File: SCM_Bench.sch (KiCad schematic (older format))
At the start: 22 parts, among them J1 Conn_Coaxial, J101 Conn_02x20_Odd_Even, J102 Conn_02x07_Odd_Even, J103 Conn_02x07_Odd_Even, J2 Conn_Coaxial, J3 Conn_Coaxial, J4 Conn_Coaxial, J5 Conn_Coaxial, J6 Conn_Coaxial, SW101 SW_Push, U101 ASDMB-xxxMHz

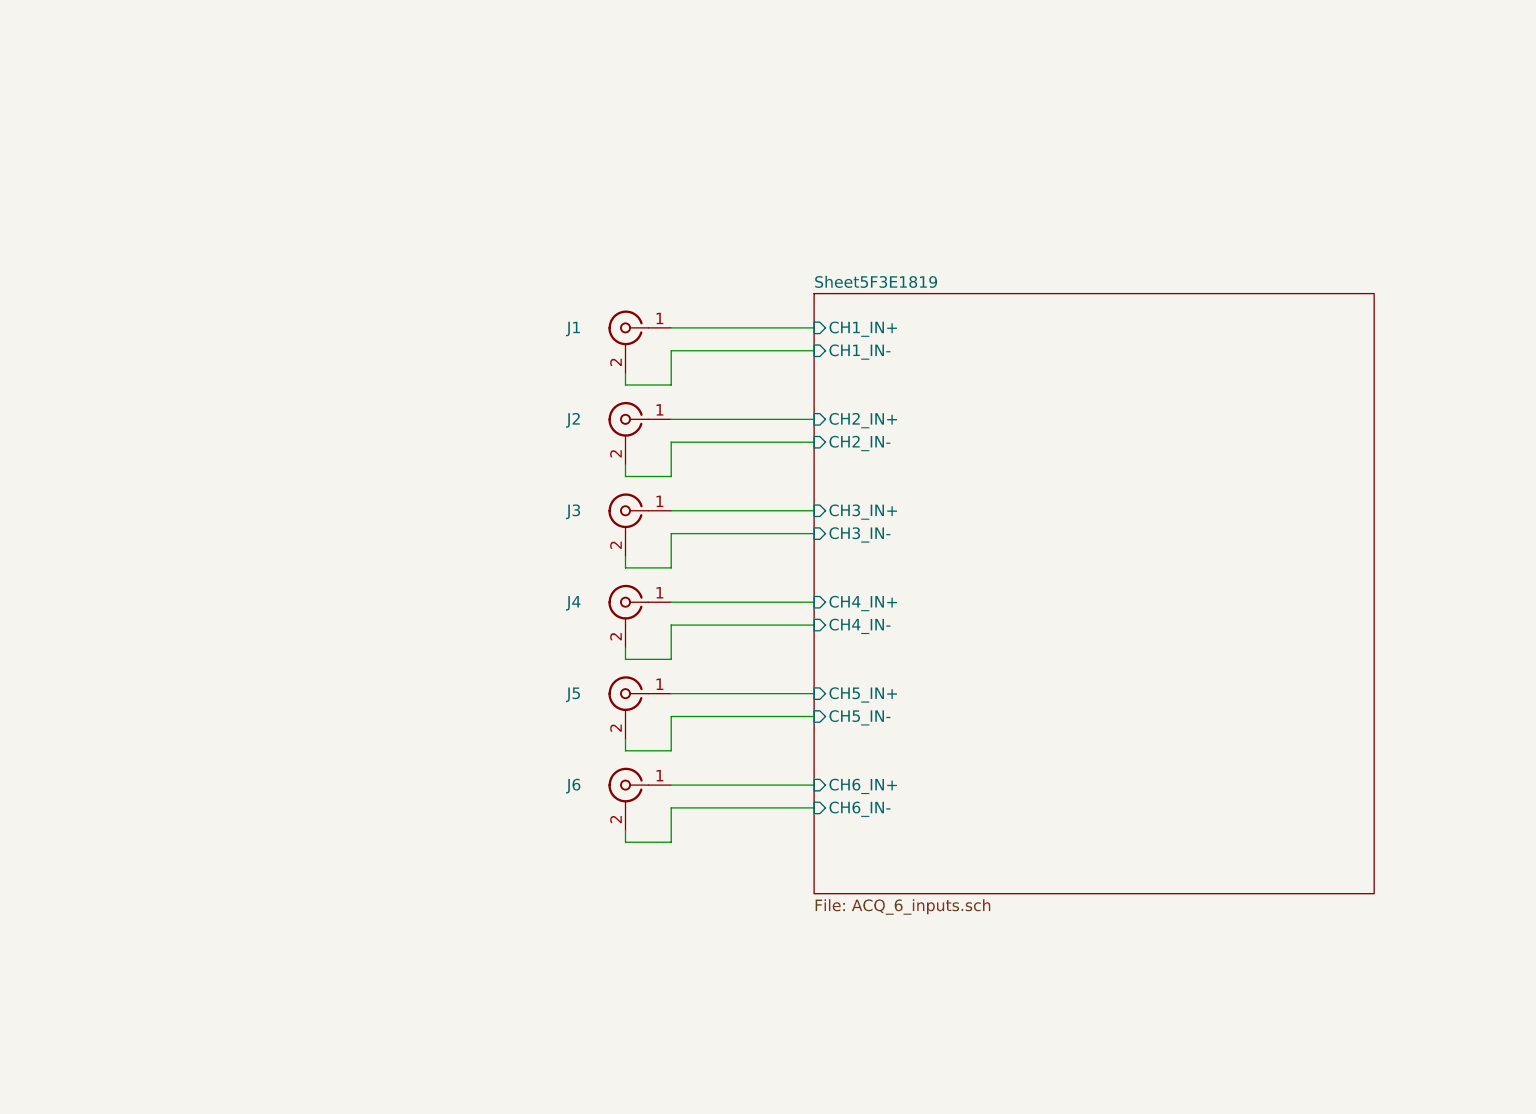
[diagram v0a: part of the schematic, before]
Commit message: Layout done for ADC + LVDS and DAC -> FPGA
Signed-off-by: Alexis Jeandet <alexis.jeandet@member.fsf.org>
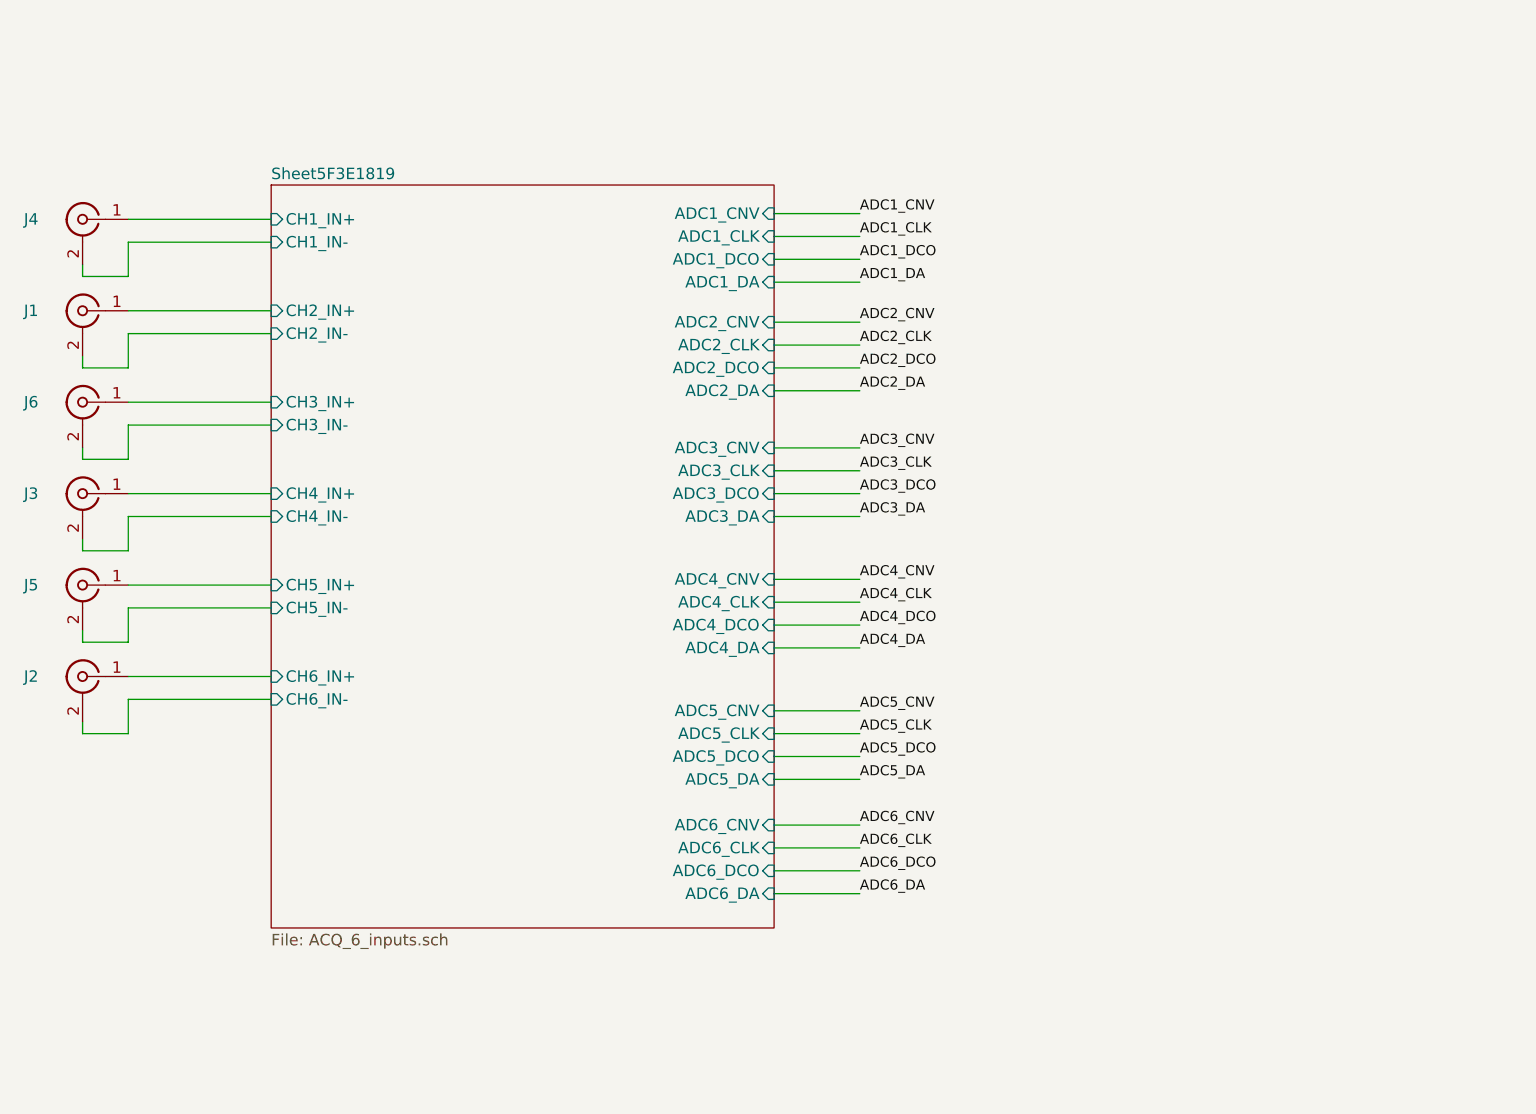
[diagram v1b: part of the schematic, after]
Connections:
- net Sheet5F3E1819/CH1_IN+: now also J4.1 (In); no longer J1.1 (In)
- net Sheet5F3E1819/CH1_IN-: now also J4.2 (Ext); no longer J1.2 (Ext)
- net Sheet5F3E1819/CH2_IN+: now also J1.1 (In); no longer J2.1 (In)
- net Sheet5F3E1819/CH2_IN-: now also J1.2 (Ext); no longer J2.2 (Ext)
- net Sheet5F3E1819/CH3_IN+: now also J6.1 (In); no longer J3.1 (In)
- net Sheet5F3E1819/CH3_IN-: now also J6.2 (Ext); no longer J3.2 (Ext)
- net Sheet5F3E1819/CH4_IN+: now also J3.1 (In); no longer J4.1 (In)
- net Sheet5F3E1819/CH4_IN-: now also J3.2 (Ext); no longer J4.2 (Ext)
- net Sheet5F3E1819/CH6_IN+: now also J2.1 (In); no longer J6.1 (In)
- net Sheet5F3E1819/CH6_IN-: now also J2.2 (Ext); no longer J6.2 (Ext)
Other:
- moved on the sheet: J1, J2, J3, J4, J5, J6

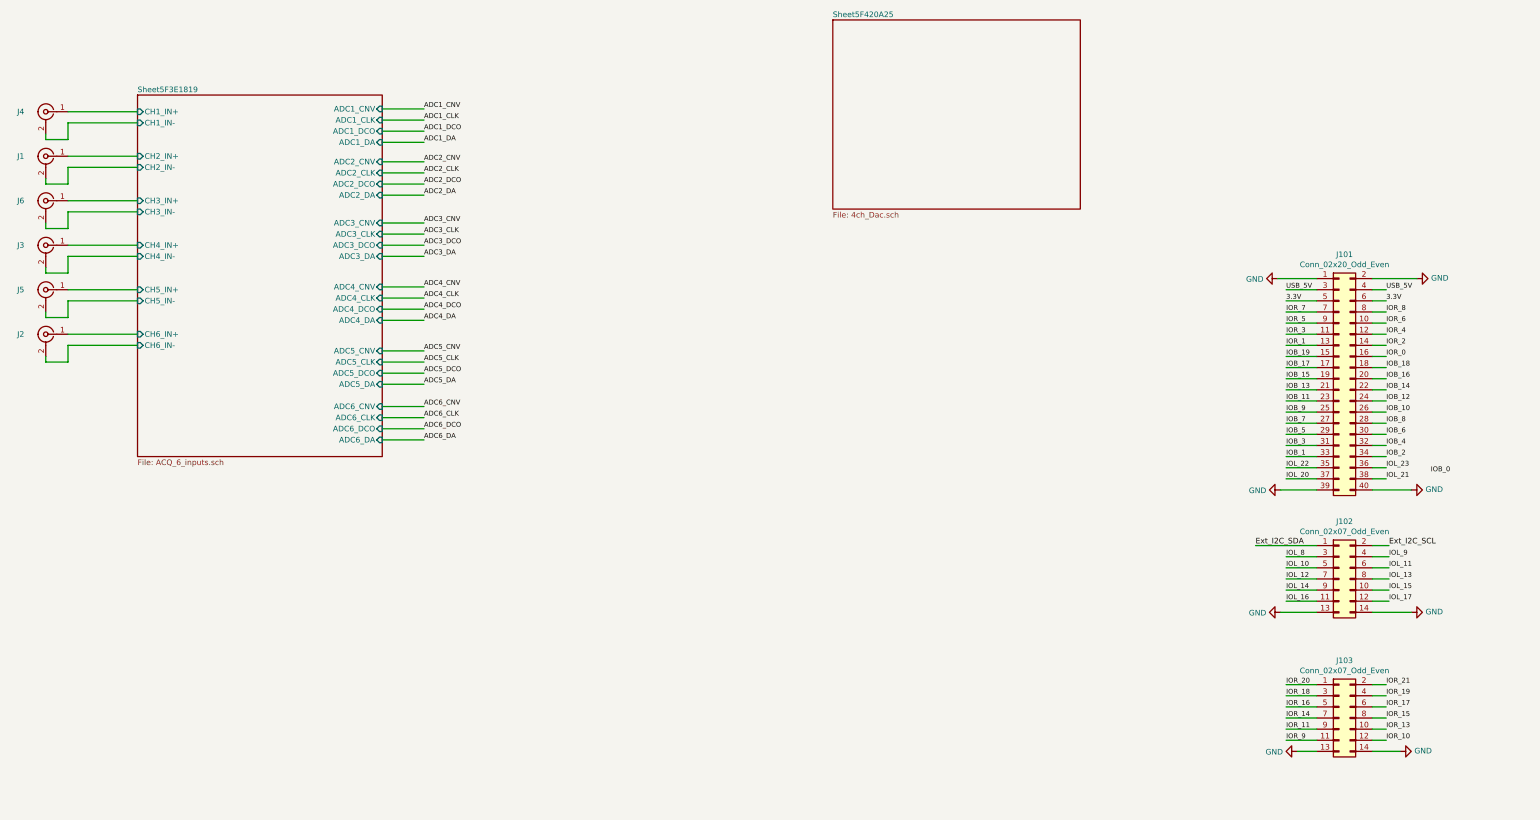
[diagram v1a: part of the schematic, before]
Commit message: Added #3.3V and #1.2V supply, completed ADC to USB board layout, added DAC FPGA to USB board bus.
Signed-off-by: Alexis Jeandet <alexis.jeandet@member.fsf.org>
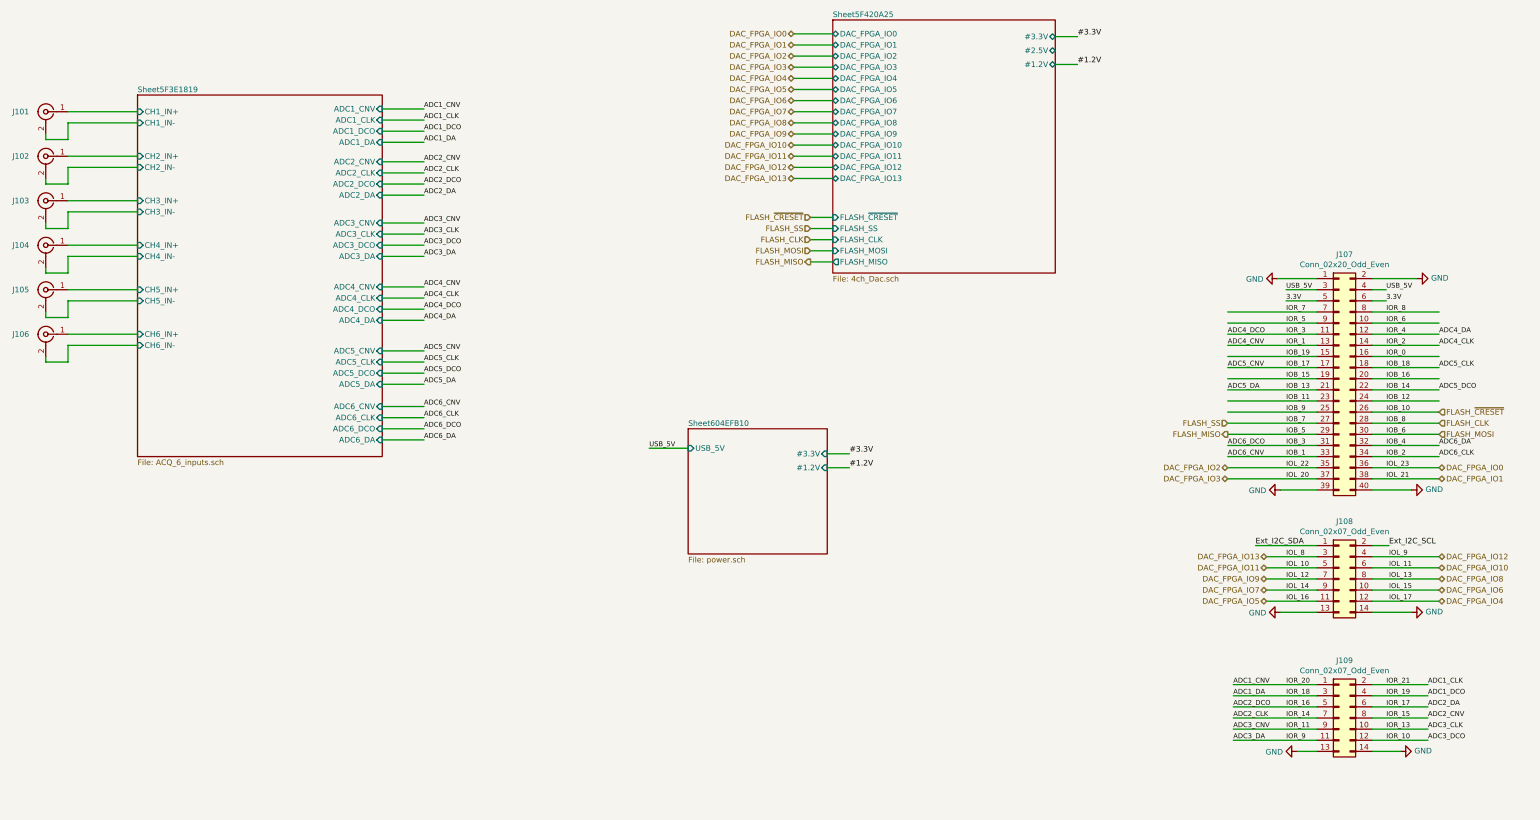
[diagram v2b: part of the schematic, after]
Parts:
- renumbered J4 to J101, J1 to J102, J6 to J103, J3 to J104, J5 to J105, J2 to J106, J101 to J107, J102 to J108, J103 to J109
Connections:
- net labels added: #1.2V, #3.3V, DAC_FPGA_IO0, DAC_FPGA_IO1, DAC_FPGA_IO10, DAC_FPGA_IO11, DAC_FPGA_IO12, DAC_FPGA_IO13, DAC_FPGA_IO2, DAC_FPGA_IO3, DAC_FPGA_IO4, DAC_FPGA_IO5, DAC_FPGA_IO6, DAC_FPGA_IO7, DAC_FPGA_IO8, DAC_FPGA_IO9, FLASH_CLK, FLASH_MISO, FLASH_MOSI, FLASH_SS, FLASH_~CRESET
- net labels removed: IOB_0
- wire segments 150 -> 174

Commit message: Layout complete, needs silk screen cleanup and few checks
Signed-off-by: Alexis Jeandet <alexis.jeandet@member.fsf.org>
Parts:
- removed C101, C102: 100nF, Capacitor_SMD:C_0402_1005Metric, symbol Device:C
- removed D101, D102: LED, Resistor_SMD:R_0603_1608Metric_Pad1.05x0.95mm_HandSolder, symbol Device:LED
- removed H101, H102: MountingHole, MountingHole:MountingHole_2.7mm_M2.5, symbol Mechanical:MountingHole
- removed R101, R102, R103: 2K2, Resistor_SMD:R_0402_1005Metric, symbol Device:R
- removed SW101: SW_Push, Button_Switch_SMD:SW_SPST_EVQPE1, symbol Switch:SW_Push
- removed U101: ASDMB-xxxMHz, Oscillator:Oscillator_SMD_Abracon_ASDMB-4Pin_2.5x2.0mm, symbol Oscillator:ASDMB-xxxMHz
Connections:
- net labels added: #1.8V, #2.5V, -5V, 2.5V, 5V, USB_3.3V
- wire segments 174 -> 161
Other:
- note added: "ADCs"
- note added: "DACs"
- note added: "PSU"
- note removed: "TBC"
- moved on the sheet: J101, J102, J103, J104, J105, J106, J107, J108, J109

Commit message: PCB ready for review
Signed-off-by: Alexis Jeandet <alexis.jeandet@member.fsf.org>
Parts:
- added J110, J111: Conn_Coaxial, Connector_Coaxial:SMB_Jack_Vertical, symbol Connector:Conn_Coaxial
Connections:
- net labels added: TRIG_IN, TRIG_OUT
- wire segments 161 -> 165
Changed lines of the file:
@@
 Text Notes 5325 1475 0    157  ~ 31
 PSU
+$Comp
+L Connector:Conn_Coaxial J111
+U 1 1 611F1260
+P 6025 5725
+F 0 "J111" H 6250 5725 50  0000 C CNN
+F 1 "Conn_Coaxial" H 6400 5725 50  0001 C CNN
+F 2 "Connector_Coaxial:SMB_Jack_Vertical" H 6025 5725 50  0001 C CNN
+F 3 " ~" H 6025 5725 50  0001 C CNN
+	1    6025 5725
+	-1   0    0    -1
+$EndComp
+$Comp
+L Connector:Conn_Coaxial J110
+U 1 1 611F126A
+P 6025 5075
+F 0 "J110" H 6250 5075 50  0000 C CNN
+F 1 "Conn_Coaxial" H 6400 5075 50  0001 C CNN
+F 2 "Connector_Coaxial:SMB_Jack_Vertical" H 6025 5075 50  0001 C CNN
+F 3 " ~" H 6025 5075 50  0001 C CNN
+	1    6025 5075
+	-1   0    0    -1
+$EndComp
+$Comp
+L power:GND #PWR0102
+U 1 1 6120BD6A
+P 6025 5975
+F 0 "#PWR0102" H 6025 5725 50  0001 C CNN
+F 1 "GND" H 6100 5825 50  0000 R CNN
+F 2 "" H 6025 5975 50  0001 C CNN
+F 3 "" H 6025 5975 50  0001 C CNN
+	1    6025 5975
+	1    0    0    -1
+$EndComp
+Wire Wire Line
+	6025 5975 6025 5925
+$Comp
+L power:GND #PWR0101
+U 1 1 61224983
+P 6025 5375
+F 0 "#PWR0101" H 6025 5125 50  0001 C CNN
+F 1 "GND" H 6100 5225 50  0000 R CNN
+F 2 "" H 6025 5375 50  0001 C CNN
+F 3 "" H 6025 5375 50  0001 C CNN
+	1    6025 5375
+	1    0    0    -1
+$EndComp
+Wire Wire Line
+	6025 5275 6025 5375
+Wire Wire Line
+	6225 5075 6400 5075
+Text Label 6400 5075 0    50   ~ 0
+TRIG_IN
+Wire Wire Line
+	6225 5725 6400 5725
+Text Label 6400 5725 0    50   ~ 0
+TRIG_OUT
+Text Label 8400 2650 0    50   ~ 0
+TRIG_IN
+Text Label 8400 2850 0    50   ~ 0
+TRIG_OUT
 $EndSCHEMATC
